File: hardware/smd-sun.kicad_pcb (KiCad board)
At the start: 2 copper layers, 50 x 50 mm, 19 parts, among them U1 NE555, U2 4017

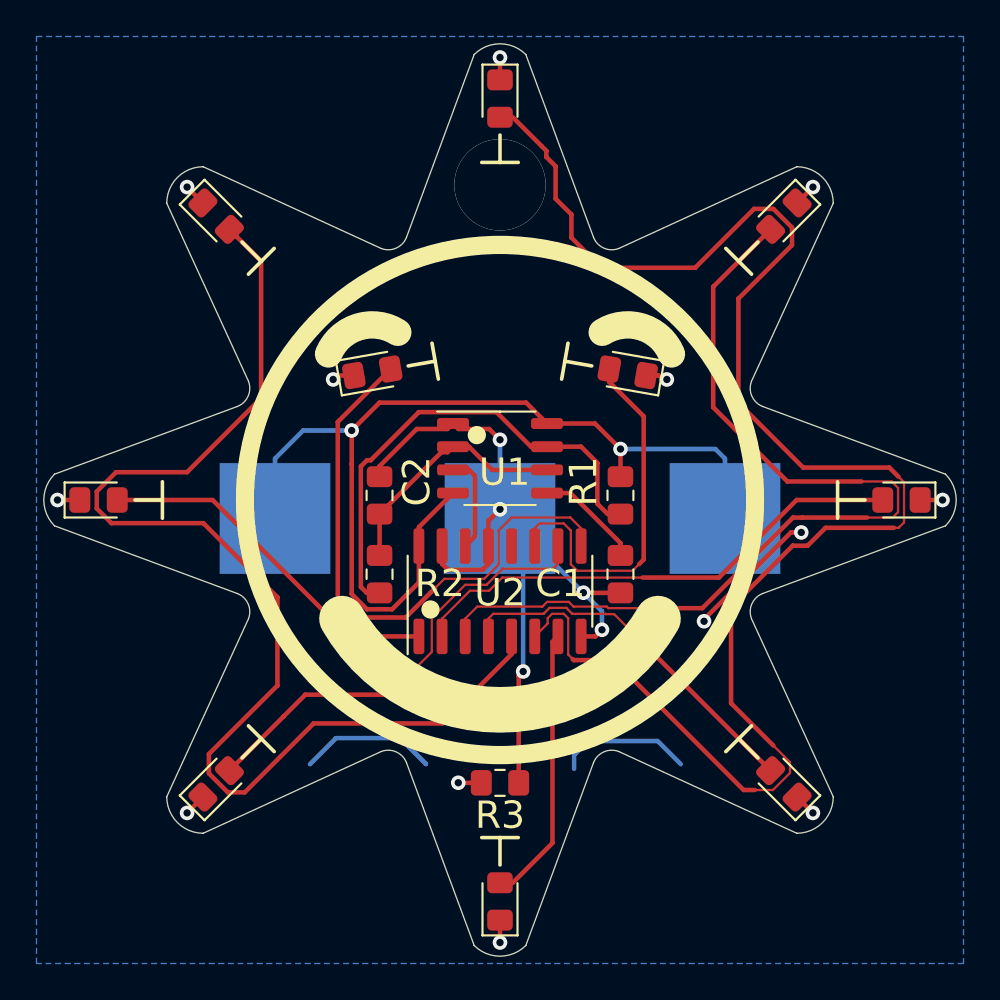
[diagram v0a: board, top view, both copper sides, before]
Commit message: Updates to July2020 pcb - fix silk clash on bottom layer - add front copper pour - enlarge cr2032 centre pad - move vias awaty from cr2032 centre pad
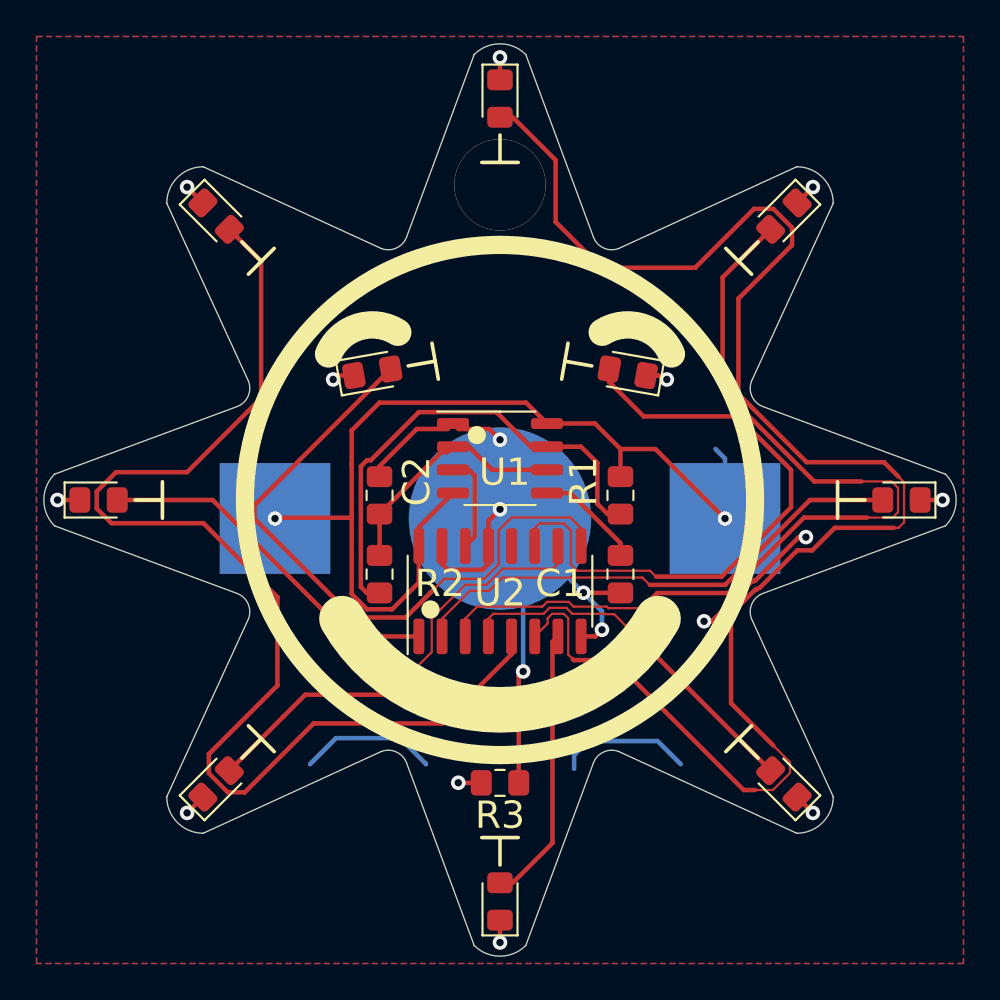
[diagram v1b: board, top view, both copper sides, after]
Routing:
- net /LED10: track 20.6 -> 33.7 mm
- net /LED9: track 32.2 -> 36.4 mm
- net +BATT: track 54.6 -> 52.8 mm
- net /LED1: track 53.5 -> 52.2 mm
- net /LED8: track 90.5 -> 90.0 mm
- added copper zone on F.Cu, net /LED_R
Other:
- board text added: "Aug2020"
- board text added: "JLCJLCJLCJLC"
- board text removed: "July2020"

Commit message: Fix resistor values Enlarge SOIC pads to make soldering easier
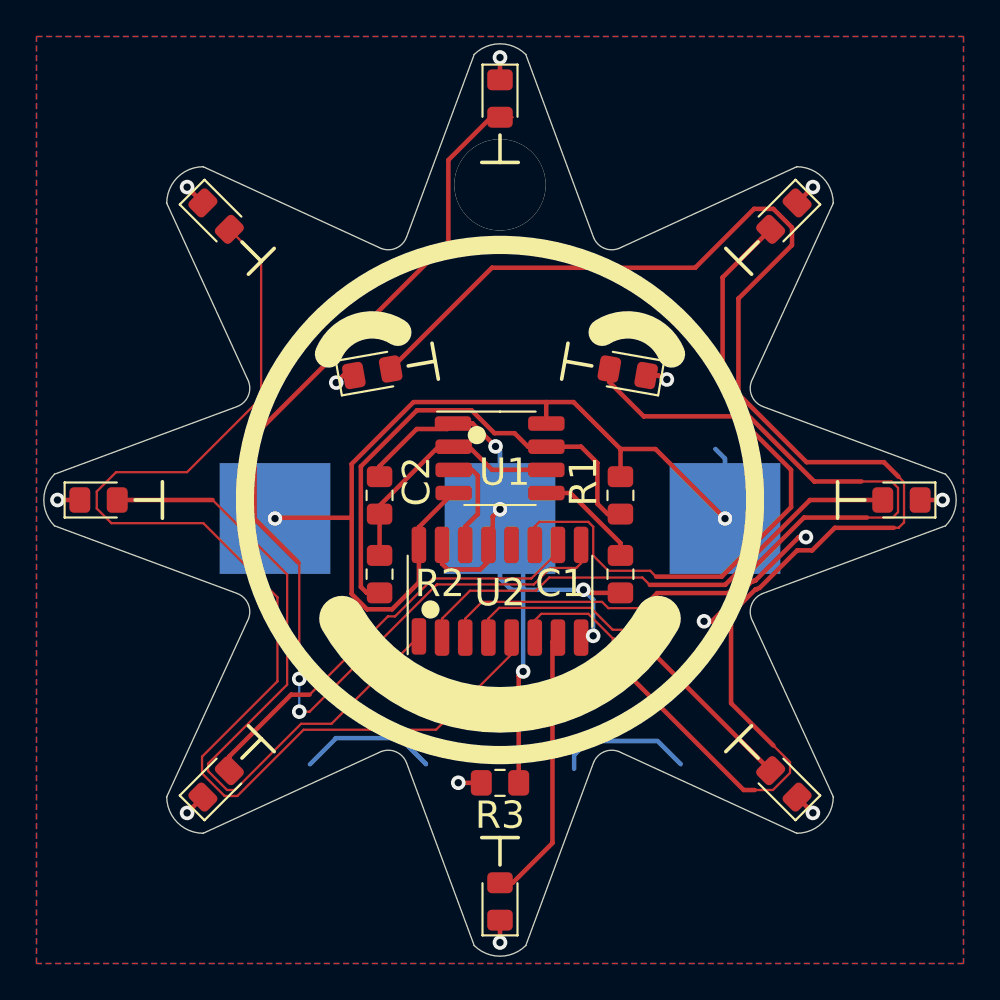
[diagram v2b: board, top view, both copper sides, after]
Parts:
- removed G***: LOGO, smd-sun:mask_600
- C1: value 0.01uF -> 10uF
- R1, R2: value 47k -> 1k
- renumbered D9 to D8, D8 to D9
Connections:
- D8 pad 2: /LED9 -> /LED8
- D9 pad 2: /LED8 -> /LED9
- U2 pad 12: (no net) -> Net-(U2-Pad12)
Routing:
- net /LED9: track 36.4 -> 60.0 mm, vias 0 -> 2
- net /LED6: track 19.6 -> 39.0 mm
- net /LED8: track 90.0 -> 92.8 mm
- net -BATT: track 47.0 -> 48.2 mm
- net /LED5: track 24.8 -> 23.8 mm
- net /LED7: track 66.3 -> 67.0 mm
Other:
- rule pad_to_mask_clearance: 0.051 -> 0
- board text added: "Dec2020"
- board text removed: "Aug2020"

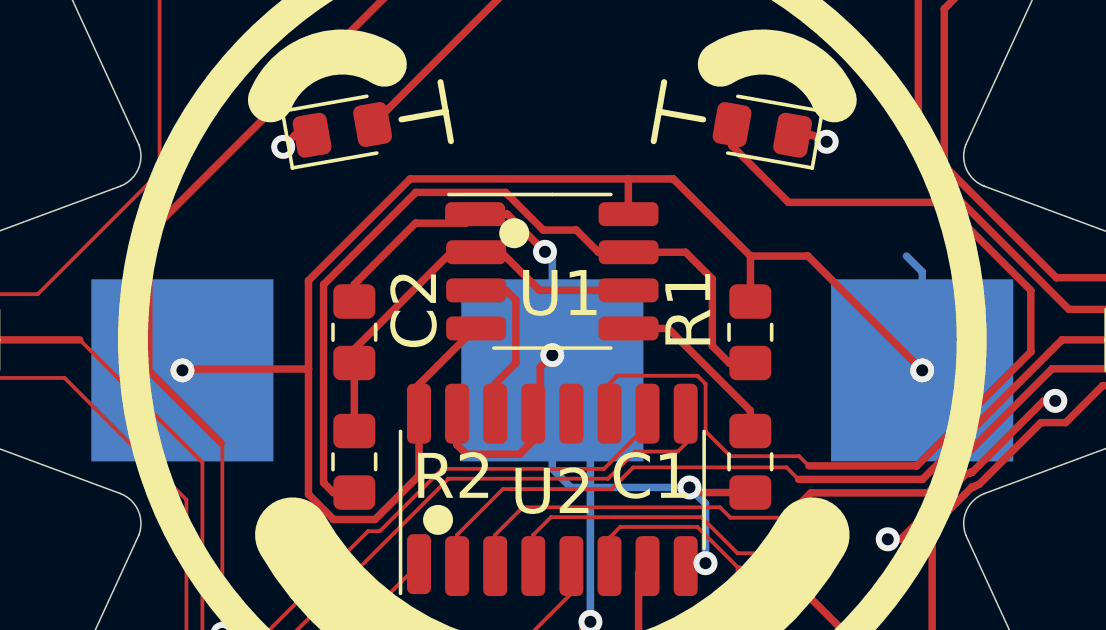
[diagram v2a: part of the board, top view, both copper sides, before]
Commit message: Add test points
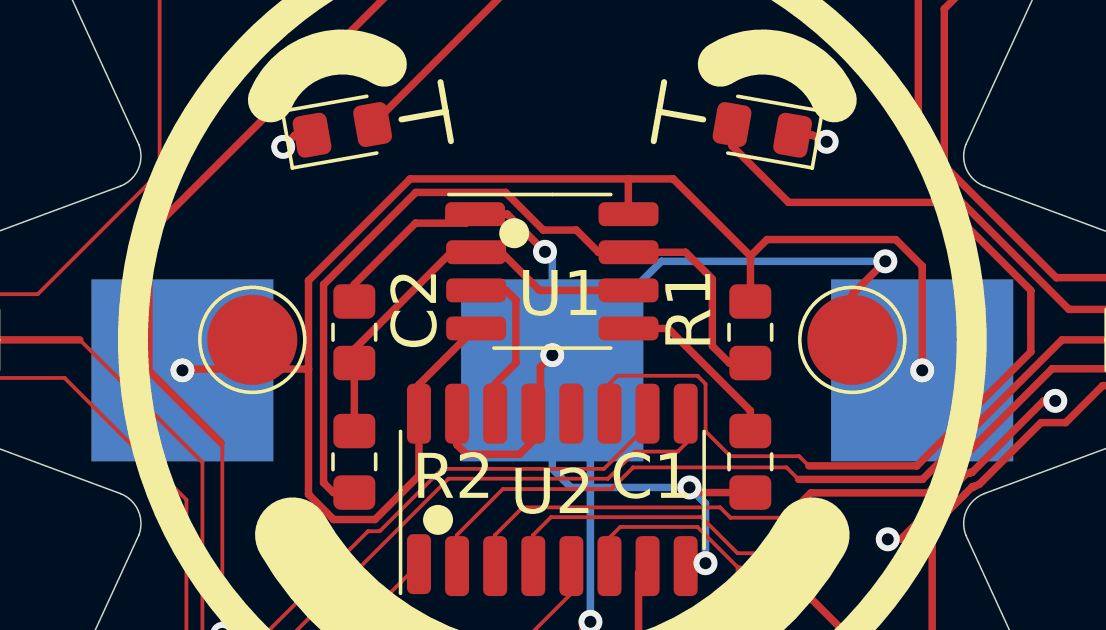
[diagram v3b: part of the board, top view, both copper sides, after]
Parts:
- added TP1: TestPoint, smd-sun:TestPoint_Pad_D3.0mm, F.Cu at (-10.0, 0.00)
- added TP2: TestPoint, smd-sun:TestPoint_Pad_D3.0mm, F.Cu at (10.0, 0.00)
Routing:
- net -BATT: track 48.2 -> 63.8 mm, vias 5 -> 6
- net +BATT: track 52.9 -> 52.3 mm

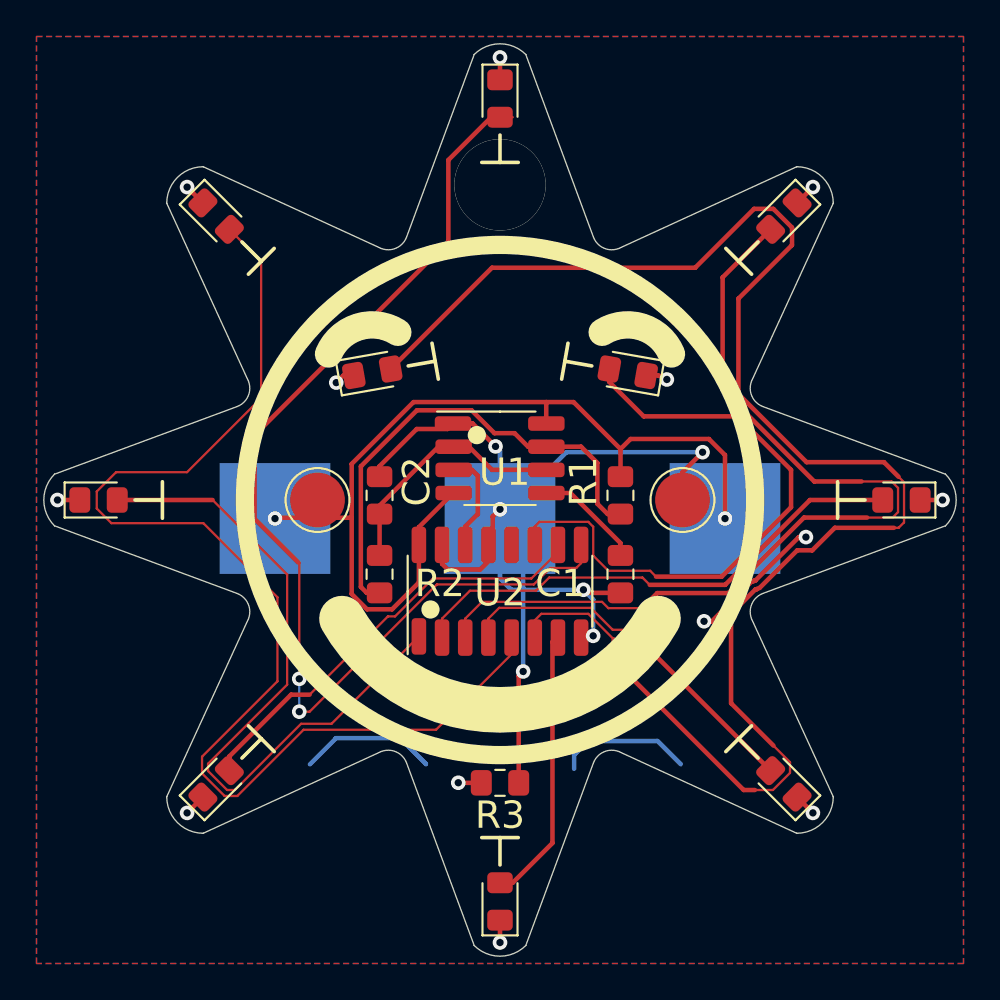
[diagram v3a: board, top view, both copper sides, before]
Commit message: Add two test point for bringup, fix errata from Jun2020
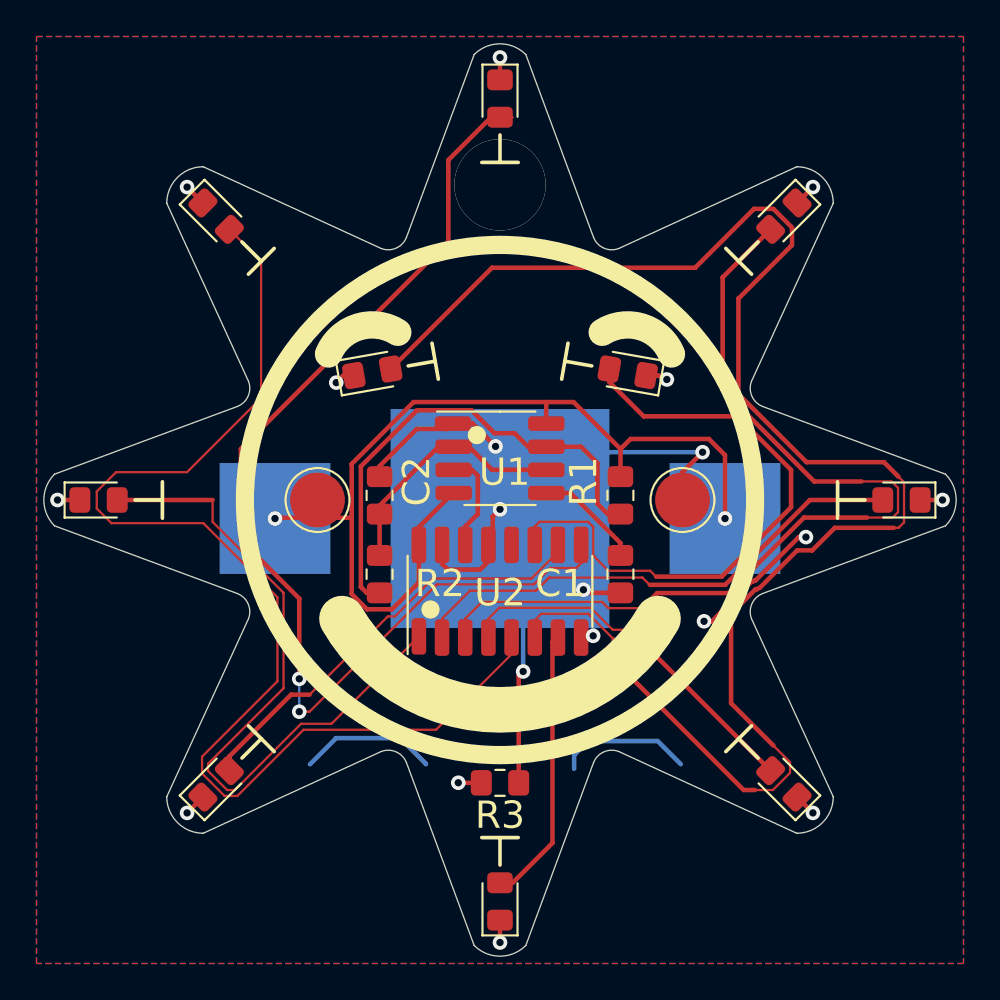
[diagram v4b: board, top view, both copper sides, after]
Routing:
- net /LED9: track 60.0 -> 60.6 mm
